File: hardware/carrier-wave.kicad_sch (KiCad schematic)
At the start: 4 parts, among them U2 OPA695, U3 THS3491, U4 AD9834, U7 TS5A3159ADCK

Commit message: Begin MCU
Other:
- added sheet Microcontroller (microcontroller.kicad_sch)
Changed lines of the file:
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@@
 	)
 	(no_connect
-		(at 45.72 45.72)
+		(at 80.645 51.435)
 	)
 	(no_connect
-		(at 45.72 43.18)
+		(at 80.645 48.895)
 	)
 	(wire
 		(pts
-			(xy 92.71 29.21) (xy 78.74 29.21)
+			(xy 189.23 34.925) (xy 175.26 34.925)
 		)
 		(stroke
@@
 	(wire
 		(pts
-			(xy 78.74 34.29) (xy 92.71 34.29)
+			(xy 175.26 40.005) (xy 189.23 40.005)
 		)
 		(stroke
@@
 	(wire
 		(pts
-			(xy 45.72 35.56) (xy 57.15 35.56)
+			(xy 80.645 41.275) (xy 93.345 41.275)
 		)
 		(stroke
@@
 	(wire
 		(pts
-			(xy 78.74 58.42) (xy 92.71 58.42)
+			(xy 175.26 64.135) (xy 189.23 64.135)
 		)
 		(stroke
@@
 	(wire
 		(pts
-			(xy 45.72 27.94) (xy 63.5 27.94)
+			(xy 80.645 33.655) (xy 99.695 33.655)
 		)
 		(stroke
@@
 	(wire
 		(pts
-			(xy 45.72 38.1) (xy 57.15 38.1)
+			(xy 80.645 43.815) (xy 93.345 43.815)
 		)
 		(stroke
@@
 	(wire
 		(pts
-			(xy 45.72 30.48) (xy 63.5 30.48)
+			(xy 80.645 36.195) (xy 99.695 36.195)
 		)
 		(stroke
@@
 	)
 	(label "USB_PWR_~{EN}"
-		(at 63.5 27.94 180)
+		(at 98.425 33.655 180)
 		(effects
 			(font
@@
 	)
 	(label "USB_D+"
-		(at 57.15 38.1 180)
+		(at 92.075 43.815 180)
 		(effects
 			(font
@@
 	)
 	(label "PWR_3.3V_EN"
-		(at 78.74 29.21 0)
+		(at 175.26 34.925 0)
 		(effects
 			(font
@@
 	)
 	(label "PWR_3.3V_PG"
-		(at 78.74 34.29 0)
+		(at 175.26 40.005 0)
 		(effects
 			(font
@@
 	)
 	(label "USB_D-"
-		(at 57.15 35.56 180)
+		(at 92.075 41.275 180)
 		(effects
 			(font
@@
 	)
 	(label "USB_PWR_~{FAULT}"
-		(at 63.5 30.48 180)
+		(at 98.425 36.195 180)
 		(effects
 			(font
@@
 	)
 	(label "PWR_12V_EN"
-		(at 78.74 58.42 0)
+		(at 175.26 64.135 0)
 		(effects
 			(font
@@
 	)
 	(sheet
-		(at 92.71 52.07)
+		(at 189.23 57.785)
 		(size 20.32 12.7)
 		(exclude_from_sim no)
@@
 		)
 		(property "Sheetname" "±12V Rail Supply"
-			(at 92.71 67.31 0)
+			(at 189.23 73.025 0)
 			(show_name no)
 			(do_not_autoplace no)
@@
 		)
 		(property "Sheetfile" "12V_boost_converter.kicad_sch"
-			(at 92.71 65.3546 0)
+			(at 189.23 71.0696 0)
 			(hide yes)
 			(show_name no)
@@
 		)
 		(property "Component" "TPS65131RGE / LM2940 & LM2990"
-			(at 110.49 50.8 0)
+			(at 207.01 56.515 0)
 			(hide yes)
 			(show_name no)
@@
 		)
 		(pin "EN" input
-			(at 92.71 58.42 180)
+			(at 189.23 64.135 180)
 			(effects
 				(font
@@
 	)
 	(sheet
-		(at 92.71 77.47)
+		(at 189.23 83.185)
 		(size 20.32 12.7)
 		(exclude_from_sim no)
@@
 		)
 		(property "Sheetname" "3.3V Digital Supply"
-			(at 92.71 92.71 0)
+			(at 189.23 98.425 0)
 			(show_name no)
 			(do_not_autoplace no)
@@
 		)
 		(property "Sheetfile" "3V_digital_supply.kicad_sch"
-			(at 92.71 90.8308 0)
+			(at 189.23 96.5458 0)
 			(hide yes)
 			(show_name no)
@@
 	)
 	(sheet
-		(at 92.71 25.4)
+		(at 189.23 31.115)
 		(size 20.32 12.7)
 		(exclude_from_sim no)
@@
 		)
 		(property "Sheetname" "±3.3V Rail Supply"
-			(at 92.71 40.64 0)
+			(at 189.23 46.355 0)
 			(show_name no)
 			(do_not_autoplace no)
@@
 		)
 		(property "Sheetfile" "charge_pump_ldo.kicad_sch"
-			(at 92.71 38.6846 0)
+			(at 189.23 44.3996 0)
 			(hide yes)
 			(show_name no)
@@
 		)
 		(pin "EN" input
-			(at 92.71 29.21 180)
+			(at 189.23 34.925 180)
 			(effects
 				(font
@@
 		)
 		(pin "PG" input
-			(at 92.71 34.29 180)
+			(at 189.23 40.005 180)
 			(effects
 				(font
@@
 	)
 	(sheet
-		(at 25.4 25.4)
+		(at 60.325 31.115)
 		(size 20.32 22.86)
 		(exclude_from_sim no)
@@
 		)
 		(property "Sheetname" "USB C Interface"
-			(at 25.4 50.8 0)
+			(at 60.325 56.515 0)
 			(show_name no)
 			(do_not_autoplace no)
@@
 		)
 		(property "Sheetfile" "usb_interface.kicad_sch"
-			(at 25.4 38.7608 0)
+			(at 60.325 44.4758 0)
 			(hide yes)
 			(show_name no)
@@
 		)
 		(pin "CC1" output
-			(at 45.72 43.18 0)
+			(at 80.645 48.895 0)
 			(effects
 				(font
@@
 		)
 		(pin "CC2" output
-			(at 45.72 45.72 0)
+			(at 80.645 51.435 0)
 			(effects
 				(font
@@
 		)
 		(pin "D+" bidirectional
-			(at 45.72 38.1 0)
+			(at 80.645 43.815 0)
 			(effects
 				(font
@@
 		)
 		(pin "D-" bidirectional
-			(at 45.72 35.56 0)
+			(at 80.645 41.275 0)
 			(effects
 				(font
@@
 		)
 		(pin "~{EN}" input
-			(at 45.72 27.94 0)
+			(at 80.645 33.655 0)
 			(effects
 				(font
@@
 		)
 		(pin "~{FAULT}" output
-			(at 45.72 30.48 0)
+			(at 80.645 36.195 0)
 			(effects
 				(font
@@
 				)
 			)
+		)
+	)
+	(sheet
+		(at 114.3 31.115)
+		(size 43.815 86.36)
+		(exclude_from_sim no)
+		(in_bom yes)
+		(on_board yes)
+		(dnp no)
+		(fields_autoplaced yes)
+		(stroke
+			(width 0.3048)
+			(type solid)
+		)
+		(fill
+			(color 255 229 191 1)
+		)
+		(property "Sheetname" "Microcontroller"
+			(at 114.3 30.3272 0)
+			(show_name no)
+			(do_not_autoplace no)
+			(effects
+				(font
+					(size 1.27 1.27)
+				)
+				(justify left bottom)
+			)
+		)
+		(property "Sheetfile" "microcontroller.kicad_sch"
+			(at 114.3 118.1358 0)
+			(hide yes)
+			(show_name no)
+			(do_not_autoplace no)
+			(effects
+				(font
+					(size 1.27 1.27)
+				)
+				(justify left top)
+			)
+		)
+		(instances
+			(project "carrier-wave"
+				(path "/dc900721-a2e3-4f11-b4f2-59bb3a47422e"
+					(page "5")
+				)
+			)

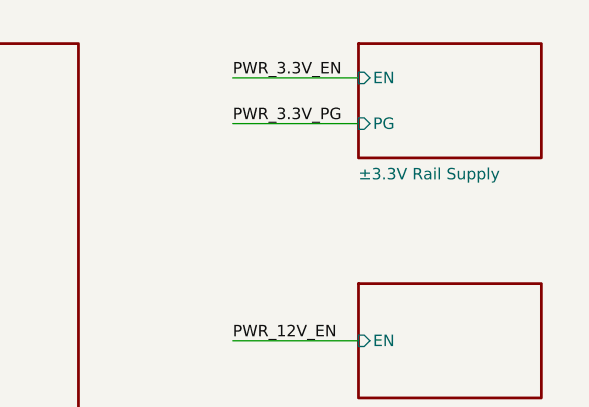
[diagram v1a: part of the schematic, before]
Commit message: Begin MCU pin assignments
Added STM32CubeMX project. Assigned peripheral pins, and began assigning GPIOs.
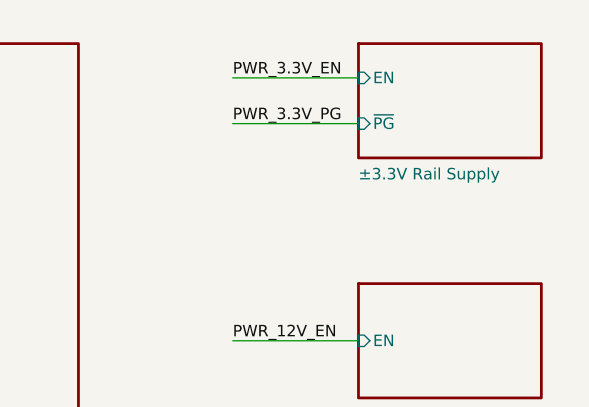
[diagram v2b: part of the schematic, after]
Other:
- sheet ±3.3V Rail Supply ports: added ~{PG}; removed PG
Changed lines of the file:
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@@
 			)
 		)
-		(pin "PG" input
+		(pin "~{PG}" input
 			(at 189.23 40.005 180)
 			(effects

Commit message: Cleanup Sheets
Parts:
- removed U2: OPA695, Package_TO_SOT_SMD:SOT-23-6, symbol carrier-wave:OPA695
- removed U3: THS3491, Package_SO:Texas_R-PDSO-G8_EP2.95x4.9mm_Mask2.4x3.1mm_ThermalVias, symbol Amplifier_Operational:THS3491xDDA
- removed U4: AD9834, Package_SO:TSSOP-20_4.4x6.5mm_P0.65mm, symbol Interface:AD9834
- removed U7: TS5A3159ADCK, Package_TO_SOT_SMD:SOT-363_SC-70-6, symbol Analog_Switch:TS5A3159ADCK
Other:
- added sheet Analog Stage (analog-stage.kicad_sch)
- added sheet User Interface (user-interface.kicad_sch)
- note removed: "Component Selection"
